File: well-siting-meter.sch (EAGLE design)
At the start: 55 parts, among them J2 7805, K1 OJE-SH-105HM,000, T1 MOSFET-NCHANNELFQP30N06L, U1 LCD-16X2NOHOLES, U2 ARDUINO_PRO_MINI, U3 EC2, U4 EC2, U5 AD623, U6 AD629, U7 MAX1771

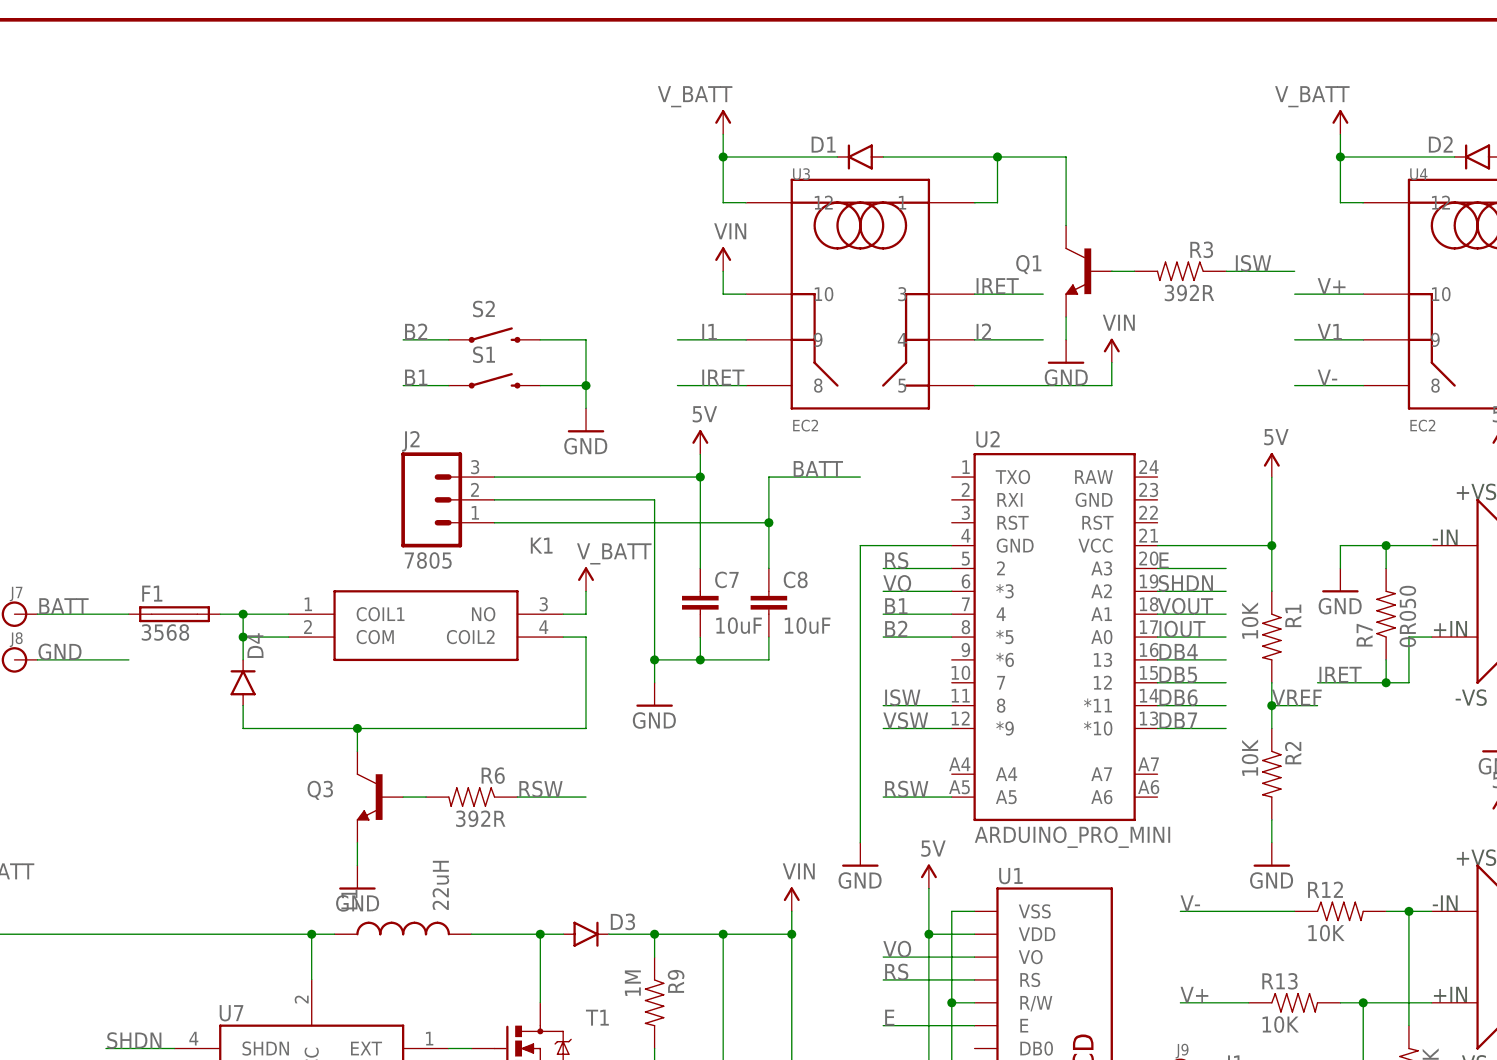
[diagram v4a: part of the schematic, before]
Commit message: adding ic1 for 2.5 vref
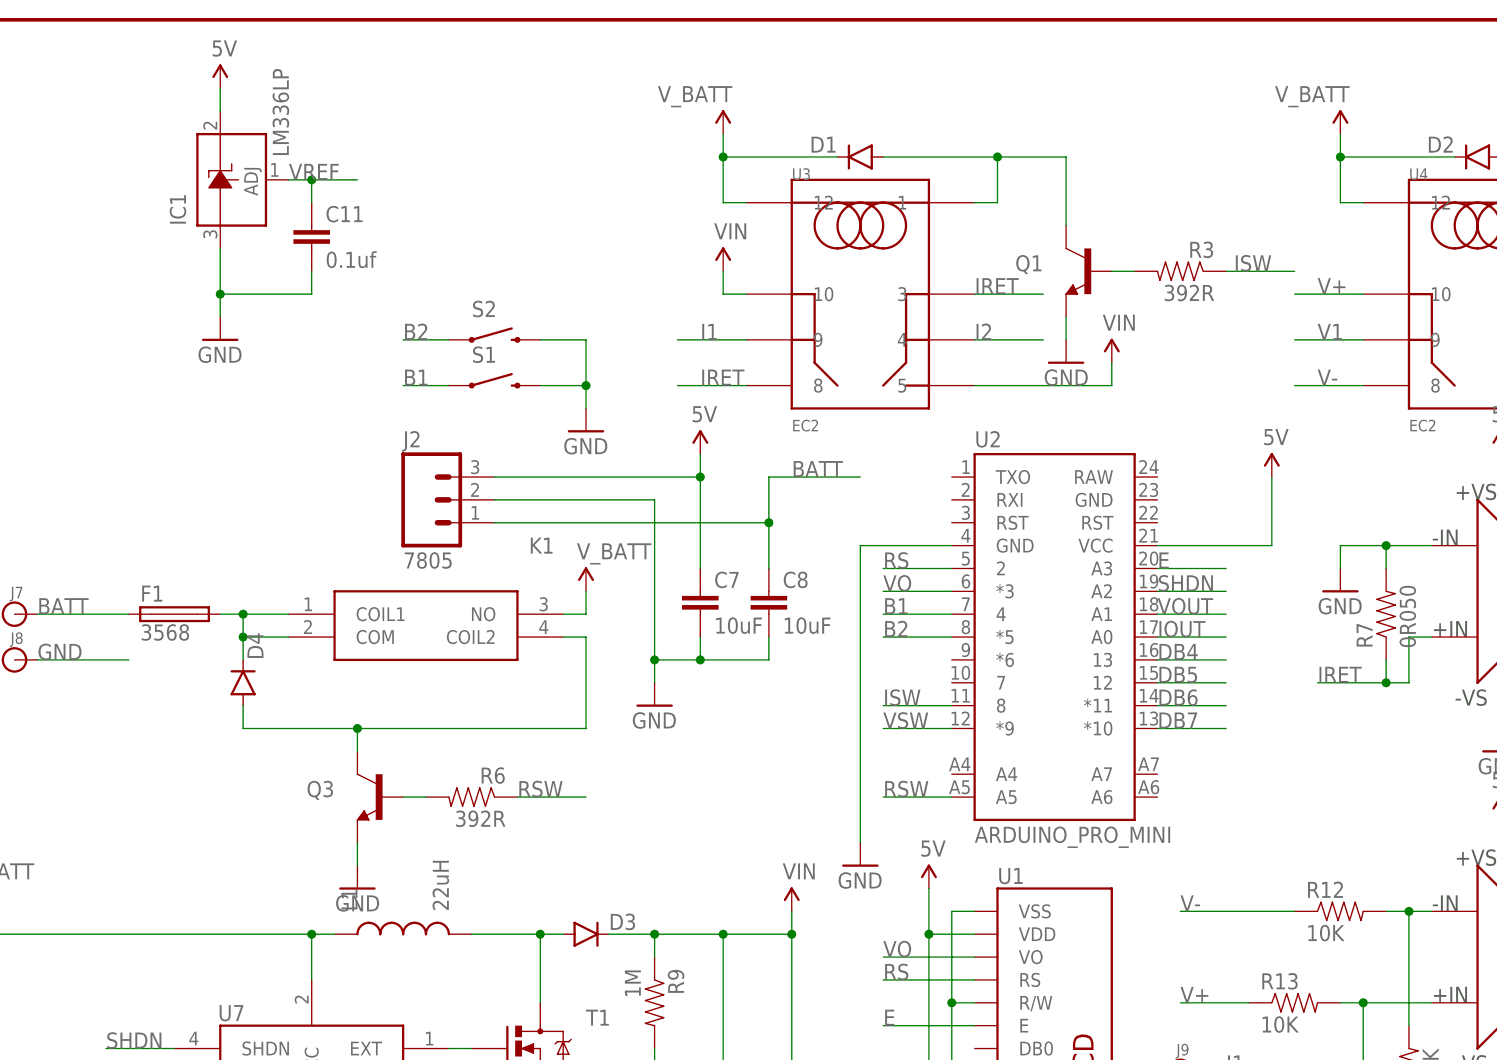
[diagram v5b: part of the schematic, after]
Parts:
- removed R1, R2: 10K, SparkFun-Passives:RESISTORPTH-1/4W
- added C11: 0.1uf, SparkFun-Passives:CAPPTH1
- added IC1: LM336LP, linear:LM336LP
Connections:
- net 5V: now also IC1.C; no longer R1.1
- net GND: now also C11.2, IC1.A; no longer R2.2
- net VREF: now also C11.1, IC1.ADJ; no longer R1.2, R2.1
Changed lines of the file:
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@@
 <attribute name="PN" value="1N4001-TPMSCT-ND"/>
-</part>
-<part name="R1" library="SparkFun-Passives" deviceset="RESISTOR" device="PTH-1/4W" value="10K">
-<attribute name="PN" value="10.0KXBK-ND"/>
-</part>
-<part name="R2" library="SparkFun-Passives" deviceset="RESISTOR" device="PTH-1/4W" value="10K">
-<attribute name="PN" value="10.0KXBK-ND"/>
 </part>
 <part name="R3" library="SparkFun-Passives" deviceset="RESISTOR" device="PTH-1/4W" value="392R">
@@
 <part name="SUPPLY12" library="SparkFun-Aesthetics" deviceset="5V" device=""/>
 <part name="GND18" library="SparkFun-Aesthetics" deviceset="GND" device=""/>
+<part name="IC1" library="linear" library_urn="urn:adsk.eagle:library:262" deviceset="LM336" device="LP" package3d_urn="urn:adsk.eagle:package:16416/2"/>
+<part name="SUPPLY14" library="SparkFun-Aesthetics" deviceset="5V" device=""/>
+<part name="C11" library="SparkFun-Passives" deviceset="CAP" device="PTH1" value="0.1uf">
+<attribute name="PN" value="BC2665CT-ND"/>
+</part>
 </parts>
 <sheets>
@@
 <attribute name="PN" x="193.04" y="170.18" size="1.778" layer="96" rot="MR0" display="off"/>
 </instance>
-<instance part="R1" gate="G$1" x="170.18" y="116.84" rot="R270">
-<attribute name="PN" x="170.18" y="116.84" size="1.778" layer="96" rot="R270" display="off"/>
-</instance>
-<instance part="R2" gate="G$1" x="170.18" y="101.6" rot="R270">
-<attribute name="PN" x="170.18" y="101.6" size="1.778" layer="96" rot="R270" display="off"/>
-</instance>
 <instance part="R3" gate="G$1" x="160.02" y="157.48" rot="MR0">
 <attribute name="PN" x="160.02" y="157.48" size="1.778" layer="96" rot="MR0" display="off"/>
@@
 </instance>
 <instance part="SUPPLY2" gate="G$1" x="170.18" y="134.62"/>
-<instance part="GND2" gate="1" x="170.18" y="91.44"/>
+<instance part="GND2" gate="1" x="53.34" y="149.86"/>
 <instance part="GND3" gate="1" x="147.32" y="147.32" rot="MR0"/>
 <instance part="GND4" gate="1" x="215.9" y="147.32" rot="MR0"/>
@@
 <instance part="SUPPLY12" gate="G$1" x="238.76" y="81.28"/>
 <instance part="GND18" gate="1" x="238.76" y="66.04"/>
+<instance part="IC1" gate="G$1" x="53.34" y="167.64" rot="R90"/>
+<instance part="SUPPLY14" gate="G$1" x="53.34" y="177.8"/>
+<instance part="C11" gate="G$1" x="63.5" y="160.02">
+<attribute name="PN" x="63.5" y="160.02" size="1.778" layer="96" display="off"/>
+</instance>
 </instances>
 <busses>
@@
 <pinref part="GND7" gate="1" pin="GND"/>
 <wire x1="195.58" y1="68.58" x2="195.58" y2="66.04" width="0.1524" layer="91"/>
-</segment>
-<segment>
-<pinref part="R2" gate="G$1" pin="2"/>
-<pinref part="GND2" gate="1" pin="GND"/>
-<wire x1="170.18" y1="93.98" x2="170.18" y2="96.52" width="0.1524" layer="91"/>
 </segment>
 <segment>
@@
 <wire x1="238.76" y1="71.12" x2="238.76" y2="68.58" width="0.1524" layer="91"/>
 </segment>
+<segment>
+<pinref part="IC1" gate="G$1" pin="A"/>
+<pinref part="GND2" gate="1" pin="GND"/>
+<wire x1="53.34" y1="160.02" x2="53.34" y2="154.94" width="0.1524" layer="91"/>
+<junction x="53.34" y="154.94"/>
+<wire x1="53.34" y1="154.94" x2="53.34" y2="152.4" width="0.1524" layer="91"/>
+<pinref part="C11" gate="G$1" pin="2"/>
+<wire x1="53.34" y1="154.94" x2="63.5" y2="154.94" width="0.1524" layer="91"/>
+<wire x1="63.5" y1="154.94" x2="63.5" y2="157.48" width="0.1524" layer="91"/>
+</segment>
 </net>
 <net name="5V" class="0">
@@
 <wire x1="170.18" y1="127" x2="170.18" y2="134.62" width="0.1524" layer="91"/>
 <pinref part="SUPPLY2" gate="G$1" pin="5V"/>
-<wire x1="170.18" y1="127" x2="170.18" y2="121.92" width="0.1524" layer="91"/>
-<pinref part="R1" gate="G$1" pin="1"/>
-<junction x="170.18" y="127"/>
 </segment>
 <segment>
@@
 <pinref part="C5" gate="G$1" pin="1"/>
 <wire x1="238.76" y1="81.28" x2="238.76" y2="78.74" width="0.1524" layer="91"/>
+</segment>
+<segment>
+<pinref part="SUPPLY14" gate="G$1" pin="5V"/>
+<pinref part="IC1" gate="G$1" pin="C"/>
+<wire x1="53.34" y1="177.8" x2="53.34" y2="175.26" width="0.1524" layer="91"/>
 </segment>
 </net>
@@
 <net name="VREF" class="0">
 <segment>
-<pinref part="R1" gate="G$1" pin="2"/>
-<pinref part="R2" gate="G$1" pin="1"/>
-<wire x1="170.18" y1="111.76" x2="170.18" y2="109.22" width="0.1524" layer="91"/>
-<junction x="170.18" y="109.22"/>
-<wire x1="170.18" y1="109.22" x2="170.18" y2="106.68" width="0.1524" layer="91"/>
-<wire x1="170.18" y1="109.22" x2="175.26" y2="109.22" width="0.1524" layer="91"/>
-<label x="170.18" y="109.22" size="1.778" layer="95"/>
+<label x="60.96" y="167.64" size="1.778" layer="95"/>
+<pinref part="IC1" gate="G$1" pin="ADJ"/>
+<wire x1="60.96" y1="167.64" x2="63.5" y2="167.64" width="0.1524" layer="91"/>
+<junction x="63.5" y="167.64"/>
+<wire x1="63.5" y1="167.64" x2="68.58" y2="167.64" width="0.1524" layer="91"/>
+<pinref part="C11" gate="G$1" pin="1"/>
+<wire x1="63.5" y1="165.1" x2="63.5" y2="167.64" width="0.1524" layer="91"/>
 </segment>
 <segment>
@@
 </schematic>
 </drawing>
+<compatibility>
+<note version="8.2" severity="warning">
+Since Version 8.2, EAGLE supports online libraries. The ids
+of those online libraries will not be understood (or retained)
+with this version.
+</note>
+<note version="8.3" severity="warning">
+Since Version 8.3, EAGLE supports URNs for individual library
+assets (packages, symbols, and devices). The URNs of those assets
+will not be understood (or retained) with this version.
+</note>
+<note version="8.3" severity="warning">
+Since Version 8.3, EAGLE supports the association of 3D packages
+with devices in libraries, schematics, and board files. Those 3D
+packages will not be understood (or retained) with this version.
+</note>
+</compatibility>
 </eagle>

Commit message: rev B build
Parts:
- IC1: PN (none) -> LM336Z25-ND
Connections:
- net RSW: now also U2.7; no longer U2.A5
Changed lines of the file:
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@@
 <part name="SUPPLY12" library="SparkFun-Aesthetics" deviceset="5V" device=""/>
 <part name="GND18" library="SparkFun-Aesthetics" deviceset="GND" device=""/>
-<part name="IC1" library="linear" library_urn="urn:adsk.eagle:library:262" deviceset="LM336" device="LP" package3d_urn="urn:adsk.eagle:package:16416/2"/>
+<part name="IC1" library="linear" library_urn="urn:adsk.eagle:library:262" deviceset="LM336" device="LP" package3d_urn="urn:adsk.eagle:package:16416/2">
+<attribute name="PN" value="LM336Z25-ND"/>
+</part>
 <part name="SUPPLY14" library="SparkFun-Aesthetics" deviceset="5V" device=""/>
 <part name="C11" library="SparkFun-Passives" deviceset="CAP" device="PTH1" value="0.1uf">
@@
 <instance part="SUPPLY12" gate="G$1" x="238.76" y="81.28"/>
 <instance part="GND18" gate="1" x="238.76" y="66.04"/>
-<instance part="IC1" gate="G$1" x="53.34" y="167.64" rot="R90"/>
+<instance part="IC1" gate="G$1" x="53.34" y="167.64" rot="R90">
+<attribute name="PN" x="53.34" y="167.64" size="1.778" layer="96" rot="R90" display="off"/>
+</instance>
 <instance part="SUPPLY14" gate="G$1" x="53.34" y="177.8"/>
 <instance part="C11" gate="G$1" x="63.5" y="160.02">
@@
 </segment>
 <segment>
-<pinref part="U2" gate="G$1" pin="A5"/>
-<wire x1="134.62" y1="99.06" x2="127" y2="99.06" width="0.1524" layer="91"/>
-<label x="127" y="99.06" size="1.778" layer="95"/>
-</segment>
-</net>
+<pinref part="U2" gate="G$1" pin="7"/>
+<wire x1="134.62" y1="111.76" x2="127" y2="111.76" width="0.1524" layer="91"/>
+<label x="127" y="111.76" size="1.778" layer="95"/>
+</segment>
+</net>
